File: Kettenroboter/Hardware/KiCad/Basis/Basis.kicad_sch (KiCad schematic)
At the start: 3 parts, among them U2 NCP1117LPST33T3G

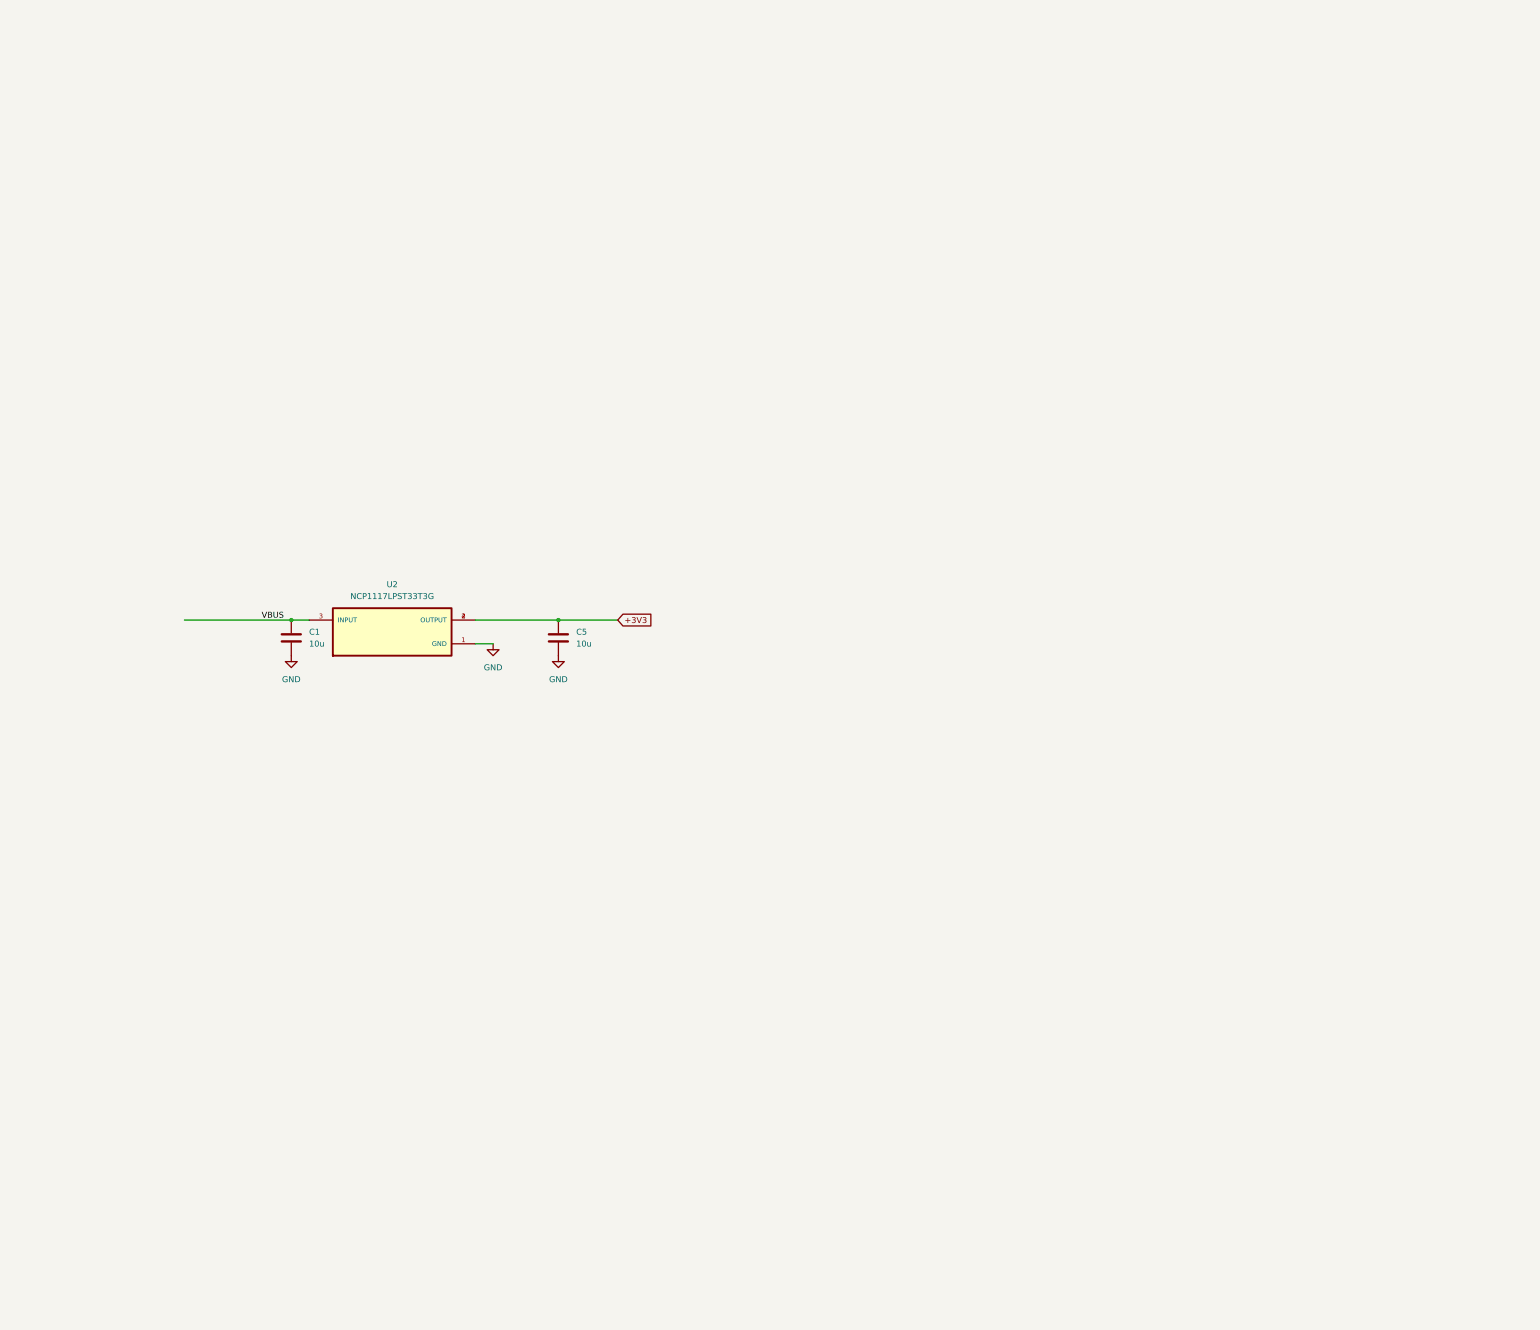
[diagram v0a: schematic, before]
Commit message: Zum Commit vorgemerkte Änderungen: 	neue Datei:     KiCad/Basis/Basis-backups/Basis-2026-01-28_145330.zip 	neue Datei:     KiCad/Basis/Basis-backups/Basis-2026-01-28_151514.zip 	neue Datei:     KiCad/Basis/Basis-backups/Basis-2026-01-28_153414.zip 	neue Datei:     KiCad/Basis/Basis-backups/Basis-2026-01-28_154223.zip 	neue Datei:     KiCad/Basis/Basis-backups/Basis-2026-01-28_155344.zip 	neue Datei:     KiCad/Basis/Basis-backups/Basis-2026-01-29_134332.zip 	neue Datei:     KiCad/Basis/Basis-backups/Basis-2026-01-29_135447.zip 	neue Datei:     KiCad/Basis/Basis-backups/Basis-2026-01-29_141859.zip 	neue Datei:     KiCad/Basis/Basis-backups/Basis-2026-01-29_143547.zip 	neue Datei:     KiCad/Basis/Basis-backups/Basis-2026-01-29_144309.zip 	neue Datei:     KiCad/Basis/Basis-backups/Basis-2026-02-04_130028.zip 	neue Datei:     KiCad/Basis/Basis-backups/Basis-2026-02-04_131400.zip 	neue Datei:     KiCad/Basis/Basis-backups/Basis-2026-02-04_132235.zip 	neue Datei:     KiCad/Basis/Basis-backups/Basis-2026-02-04_132837.zip 	neue Datei:     KiCad/Basis/Basis-backups/Basis-2026-02-04_133547.zip 	neue Datei:     KiCad/Basis/Basis-backups/Basis-2026-02-07_172846.zip 	geändert:       KiCad/Basis/Basis.kicad_pcb 	geändert:       KiCad/Basis/Basis.kicad_prl 	geändert:       KiCad/Basis/Basis.kicad_pro 	geändert:       KiCad/Basis/Basis.kicad_sch 	geändert:       KiCad/Basis/design-block-lib-table 	neue Datei:     KiCad/Basis/fp-info-cache 	neue Datei:     KiCad/Basis/fp-lib-table 	geändert:       KiCad/Basis/sym-lib-table 	geändert:       KiCad/Bausteine/Input_Supply_3V3.kicad_sch 	neue Datei:     KiCad/Bauteil-Library/Buck Converter/buck_conv_place_holder.bak 	neue Datei:     KiCad/Bauteil-Library/Buck Converter/buck_conv_place_holder.kicad_sym 	neue Datei:     KiCad/Bauteil-Library/Footprints/Library.pretty/CONN_39773-0002_MOL.kicad_mod 	neue Datei:     KiCad/Bauteil-Library/Footprints/Library.pretty/Raspberrypi pico2 THT.kicad_mod 	neue Datei:     KiCad/Bauteil-Library/Footprints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
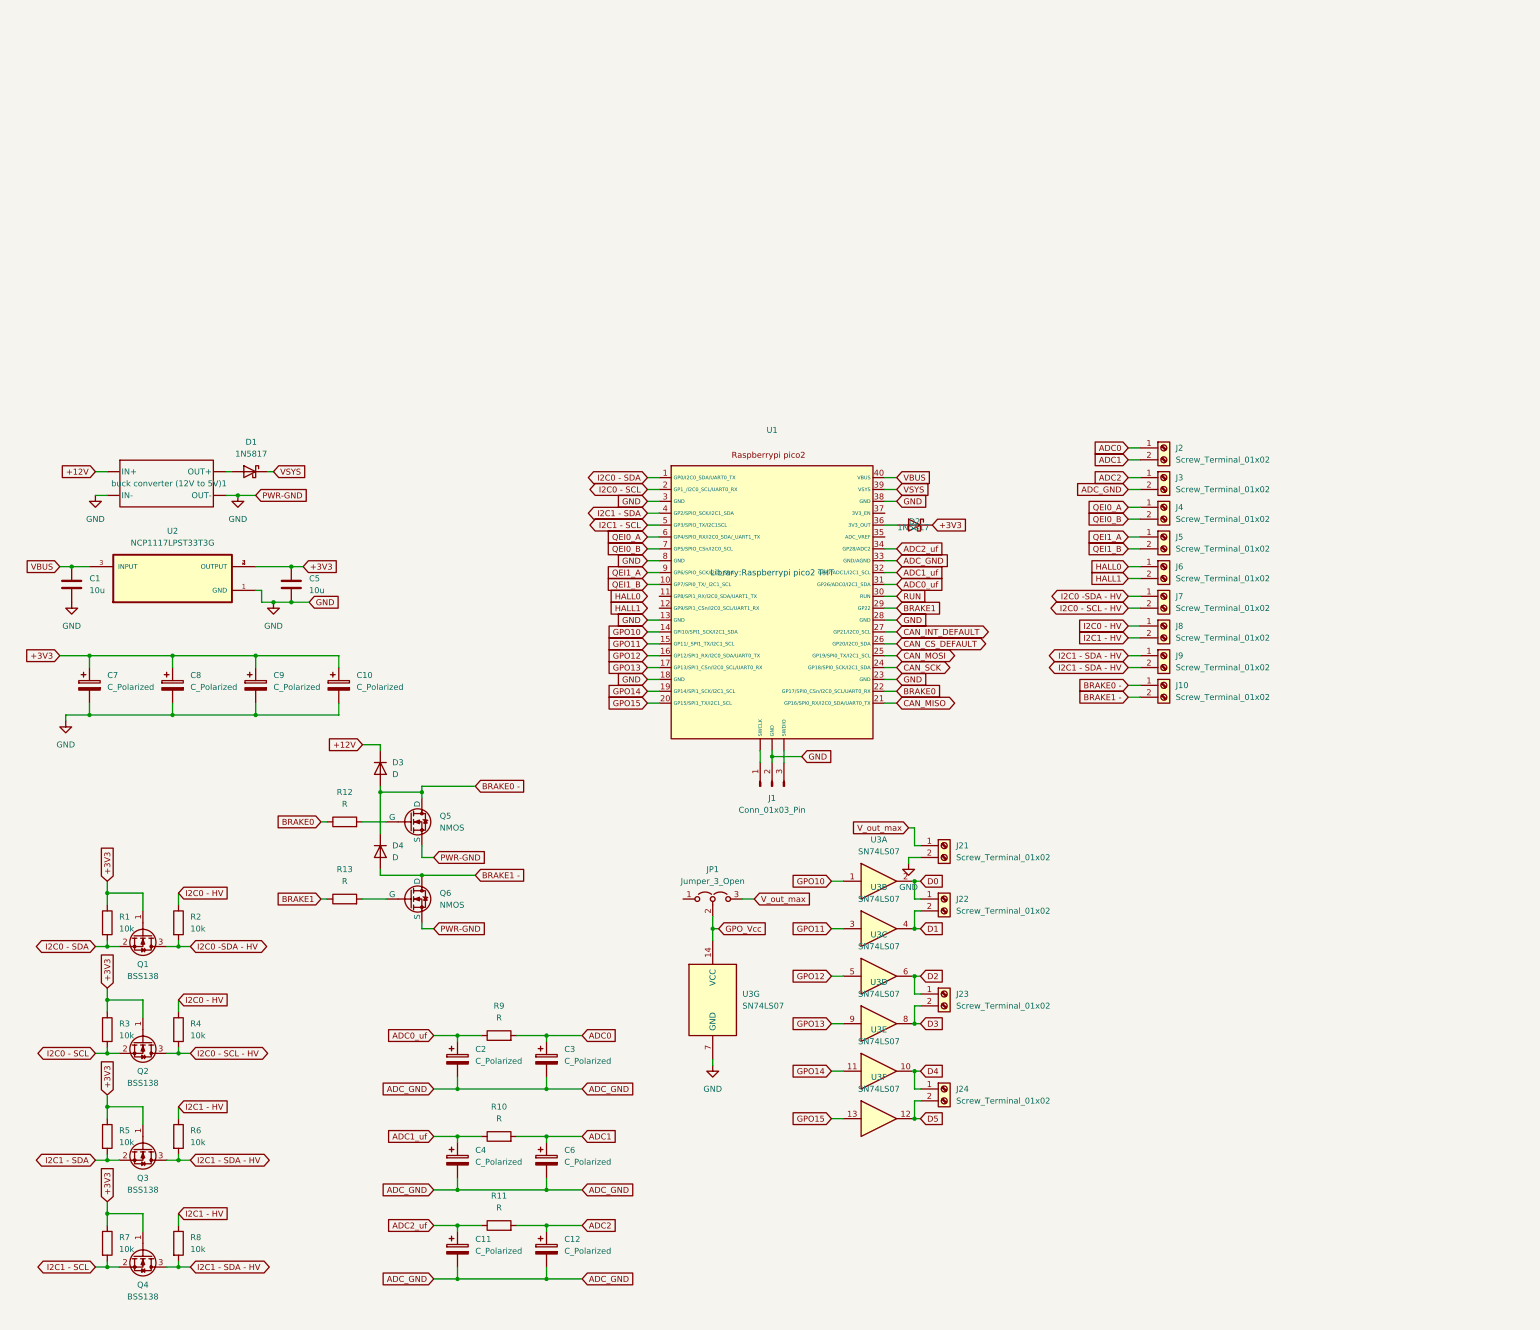
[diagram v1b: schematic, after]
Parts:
- added C10, C11, C12, C2, C3, C4, C6, C7, C8, C9: C_Polarized, symbol Device:C_Polarized
- added D1, D2: 1N5817, Diode_THT:D_DO-41_SOD81_P10.16mm_Horizontal, symbol Diode:1N5817
- added D3, D4: D, symbol Device:D
- added J1: Conn_01x03_Pin, symbol Connector:Conn_01x03_Pin
- added J10, J2, J21, J22, J23, J24, J3, J4, J5, J6, J7, J8, J9: Screw_Terminal_01x02, Library:CONN_39773-0002_MOL, symbol Connector:Screw_Terminal_01x02
- added JP1: Jumper_3_Open, symbol Jumper:Jumper_3_Open
- added Q1, Q2, Q3, Q4: BSS138, Package_TO_SOT_SMD:SOT-23, symbol Transistor_FET:BSS138
- added Q5, Q6: NMOS, Library:SOT-23_AO3400, symbol Simulation_SPICE:NMOS
- added R1, R2, R3, R4, R5, R6, R7, R8: 10k, Resistor_SMD:R_1206_3216Metric_Pad1.30x1.75mm_HandSolder, symbol Device:R
- added R10, R11, R12, R13, R9: R, Resistor_SMD:R_1206_3216Metric_Pad1.30x1.75mm_HandSolder, symbol Device:R
- added U1: ~, Library:Raspberrypi pico2 THT, symbol BA_Pico_2_W:U
- added U3: SN74LS07, Library:SOIC127P600X175-14N, symbol 74xx:SN74LS07
- added buck converter (12V to 5V)1: ~, symbol buck_conv_place_holder:buck_conv_12V_5V_ph
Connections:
- net +3V3: now also C10.1, C7.1, C8.1, C9.1, D2.1 (K), Q1.1 (G), Q2.1 (G), Q3.1 (G), Q4.1 (G), R1.1, R3.1, R5.1, R7.1
- net GND: now also C10.2, C7.2, C8.2, C9.2, J1.2 (Pin_2), J21.2 (Pin_2), Q5.3 (S), Q6.3 (S), U1. (SWDIO), U1.13 (GND), U1.18 (GND), U1.23 (GND), U1.28 (GND), U1.3 (GND), U1.38 (GND), U1.8 (GND), U3.7 (GND), buck converter (12V to 5V)1. (OUT-)
- net VBUS: now also U1.40 (VBUS)
- new net: Q5.2 (G), R12.2
- new net: J1.1 (Pin_1), U1. (SWDIO)
- new net: J1.3 (Pin_3), U1. (SWDIO)
- new net: D1.2 (A), buck converter (12V to 5V)1. (OUT-)
- new net: D2.2 (A), U1.36 (3V3_OUT)
- new net: Q6.2 (G), R13.2
- new net +12V: D3.1 (K), buck converter (12V to 5V)1. (OUT-)
- new net ADC0: C3.1, J2.1 (Pin_1), R9.2
- new net ADC0_uf: C2.1, R9.1, U1.31 (GP26/ADC0/I2C1_SDA)
- new net ADC1: C6.1, J2.2 (Pin_2), R10.2
- new net ADC1_uf: C4.1, R10.1, U1.32 (GP27/ADC1/I2C1_SCL)
- new net ADC2: C12.1, J3.1 (Pin_1), R11.2
- new net ADC2_uf: C11.1, R11.1, U1.34 (GP28/ADC2)
- new net ADC_GND: C11.2, C12.2, C2.2, C3.2, C4.2, C6.2, J3.2 (Pin_2), U1.33 (GND/AGND)
- new net BRAKE0: R12.1, U1.22 (GP17/SPI0_CSn/I2C0_SCL/UART0_RX)
- new net BRAKE0 -: D3.2 (A), D4.1 (K), J10.1 (Pin_1), Q5.1 (D)
- new net BRAKE1: R13.1, U1.29 (GP22)
- new net BRAKE1 -: D4.2 (A), J10.2 (Pin_2), Q6.1 (D)
- new net CAN_CS_DEFAULT: U1.26 (GP20/I2C0_SDA)
- new net CAN_INT_DEFAULT: U1.27 (GP21/I2C0_SCL)
- new net CAN_MISO: U1.21 (GP16/SPI0_RX/I2C0_SDA/UART0_TX)
- new net CAN_MOSI: U1.25 (GP19/SPI0_TX/I2C1_SCL)
- new net CAN_SCK: U1.24 (GP18/SPI0_SCK/I2C1_SDA)
- new net D0: J22.1 (Pin_1), U3.2
- new net D1: J22.2 (Pin_2), U3.4
- new net D2: J23.1 (Pin_1), U3.6
- new net D3: J23.2 (Pin_2), U3.8
- new net D4: J24.1 (Pin_1), U3.10
- new net D5: J24.2 (Pin_2), U3.12
- new net GPO10: U1.14 (GPI10/SPI1_SCK/I2C1_SDA), U3.1
- new net GPO11: U1.15 (GP11/_SPI1_TX/I2C1_SCL), U3.3
- new net GPO12: U1.16 (GP12/SPI1_RX/I2C0_SDA/UART0_TX), U3.5
- new net GPO13: U1.17 (GP13/SPI1_CSn/I2C0_SCL/UART0_RX), U3.9
- new net GPO14: U1.19 (GP14/SPI1_SCK/I2C1_SCL), U3.11
- new net GPO15: U1.20 (GP15/SPI1_TX/I2C1_SCL), U3.13
- new net GPO_Vcc: JP1.2 (C), U3.14 (VCC)
- new net HALL0: J6.1 (Pin_1)
- new net HALL1: J6.2 (Pin_2)
- new net I2C0 - HV: J8.1 (Pin_1), R2.1, R4.1
- new net I2C0 - SCL: Q2.2 (S), R3.2, U1.2 (GP1_/I2C0_SCL/UART0_RX)
- new net I2C0 - SCL - HV: J7.2 (Pin_2), Q2.3 (D), R4.2
- new net I2C0 - SDA: Q1.2 (S), R1.2, U1.1 (GP0/I2C0_SDA/UART0_TX)
- new net I2C0 -SDA - HV: J7.1 (Pin_1), Q1.3 (D), R2.2
- new net I2C1 - HV: J8.2 (Pin_2), R6.1, R8.1
- new net I2C1 - SCL: Q4.2 (S), R7.2, U1.5 (GP3/SPIO_TX/I2C1SCL)
- new net I2C1 - SDA: Q3.2 (S), R5.2, U1.4 (GP2/SPIO_SCK/I2C1_SDA)
- new net I2C1 - SDA - HV: J9.1 (Pin_1), J9.2 (Pin_2), Q3.3 (D), Q4.3 (D), R6.2, R8.2
- new net QEI0_A: J4.1 (Pin_1), U1.6 (GP4/SPIO_RX/I2C0_SDA/_UART1_TX)
- new net QEI0_B: J4.2 (Pin_2), U1.7 (GP5/SPIO_CSn/I2C0_SCL)
- new net QEI1_A: J5.1 (Pin_1), U1.9 (GP6/SPIO_SCK/I2C1_SDA)
- new net QEI1_B: J5.2 (Pin_2), U1.10 (GP7/SPI0_TX/_I2C1_SCL)
- new net RUN: U1.30 (RUN)
- new net VSYS: D1.1 (K), U1.39 (VSYS)
- new net V_out_max: J21.1 (Pin_1), JP1.3 (B)
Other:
- moved on the sheet: C1, C5, U2

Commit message: Nets korrigiert, etc
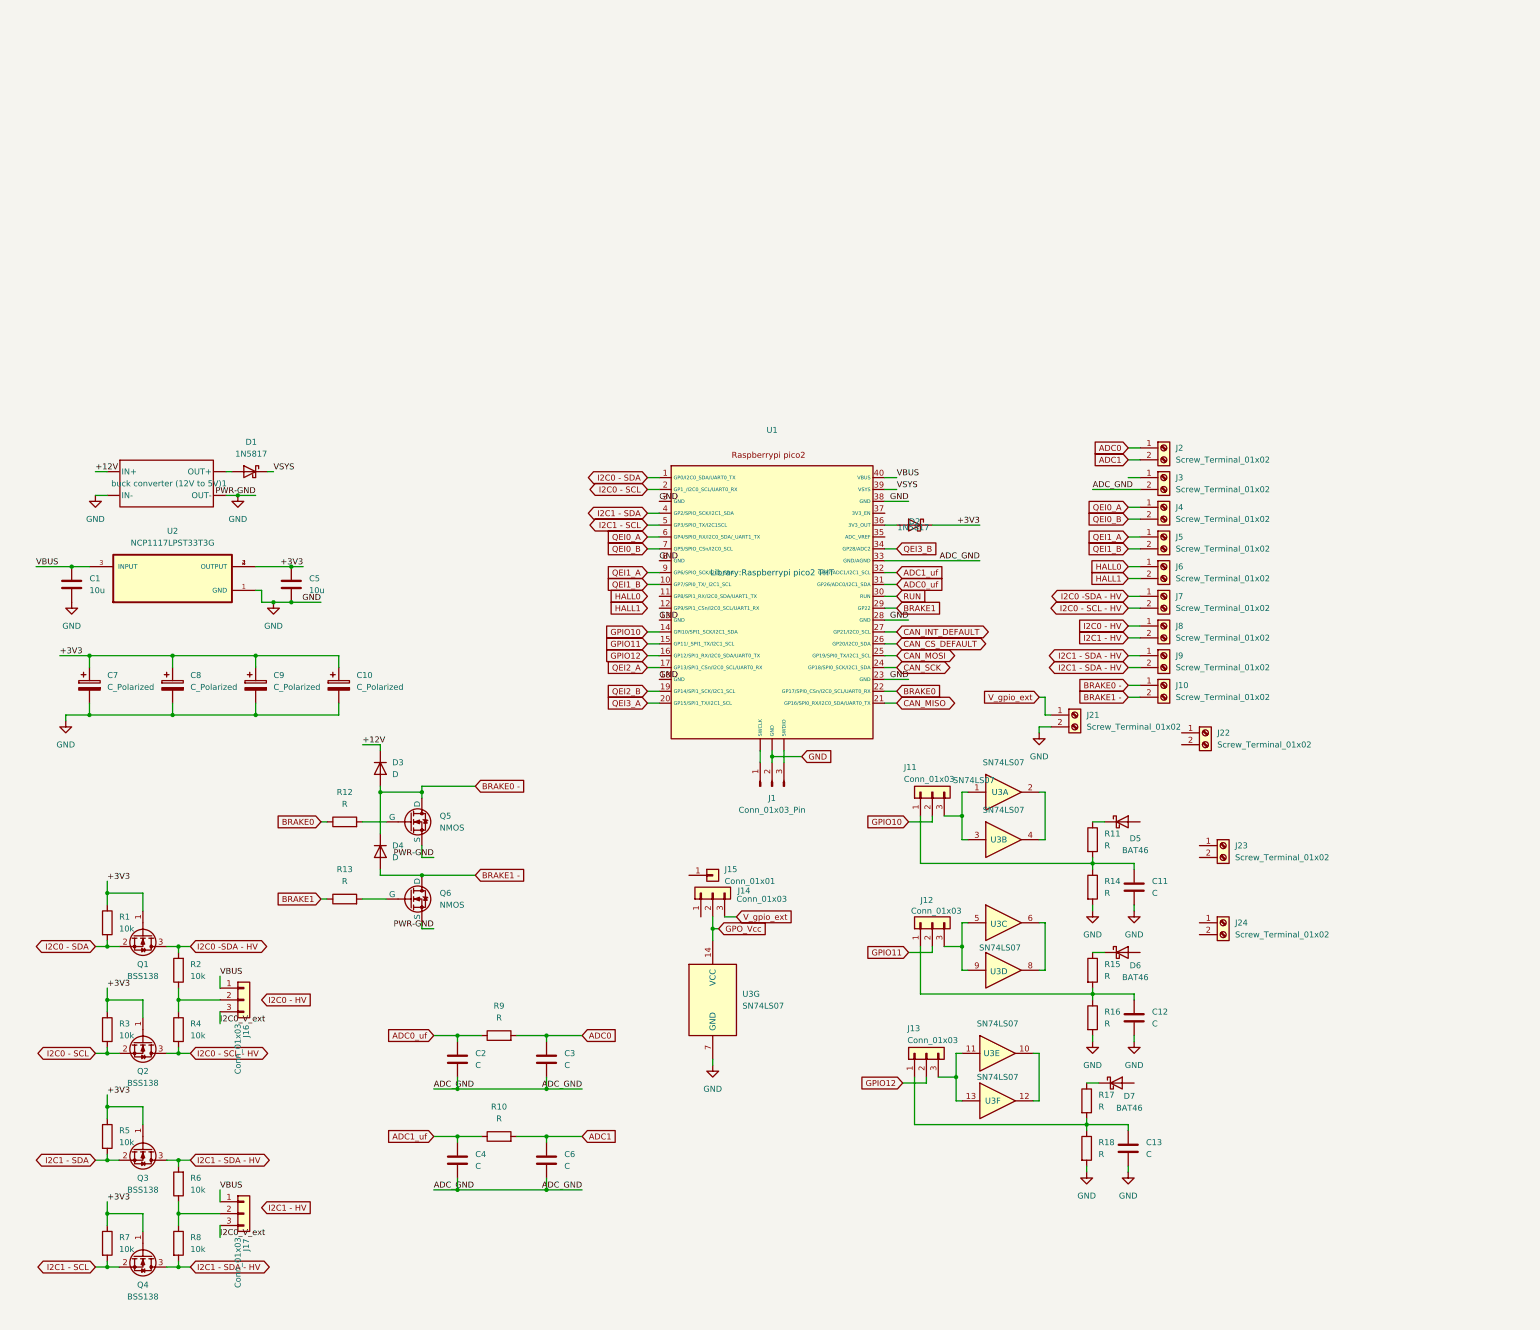
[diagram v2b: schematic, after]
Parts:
- removed C11, C12, C2, C3, C4, C6: C_Polarized, symbol Device:C_Polarized
- removed JP1: Jumper_3_Open, symbol Jumper:Jumper_3_Open
- added C11, C12, C13: C, symbol Device:C
- added C2, C3, C4, C6: C, Capacitor_SMD:C_1206_3216Metric_Pad1.33x1.80mm_HandSolder, symbol Device:C
- added D5, D6, D7: BAT46, Diode_THT:D_DO-35_SOD27_P7.62mm_Horizontal, symbol Diode:BAT46
- added J11, J12, J13, J14, J16, J17: Conn_01x03, symbol Connector_Generic:Conn_01x03
- added J15: Conn_01x01, symbol Connector_Generic:Conn_01x01
- added R14, R15, R16, R17, R18: R, symbol Device:R
- R11: footprint Resistor_SMD:R_1206_3216Metric_Pad1.30x1.75mm_HandSolder -> (none)
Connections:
- net ADC0: now also C3.1
- net ADC0_uf: now also C2.1
- net ADC1: now also C6.1
- net ADC1_uf: now also C4.1
- net ADC_GND: now also C2.2, C3.2, C4.2, C6.2
- net GND: now also C11.2, C12.2, C13.2, R14.2, R16.2, R18.2
- net GPO_Vcc: now also J14.2 (Pin_2)
- net I2C0 - HV: no longer R2.1, R4.1
- net I2C1 - HV: no longer R6.1, R8.1
- net VBUS: now also J16.1 (Pin_1), J17.1 (Pin_1)
- net ADC2: no longer names the net of R11.2
- net ADC2: now also C11.1, J11.1 (Pin_1), R14.1; no longer J3.1 (Pin_1)
- net ADC2_uf: no longer names the net of R11.1
- net ADC2_uf: now also D5.1 (K); no longer U1.34 (GP28/ADC2)
- net D0: no longer names the net of U3.2
- net D0: now also U3.4; no longer J22.1 (Pin_1)
- net D1: no longer names the net of J22.2 (Pin_2)
- net D1: no longer U3.4
- net D2: no longer names the net of U3.6
- net D2: now also U3.8; no longer J23.1 (Pin_1)
- net D3: no longer names the net of J23.2 (Pin_2)
- net D3: no longer U3.8
- net D4: no longer names the net of U3.10
- net D4: now also U3.12; no longer J24.1 (Pin_1)
- net D5: no longer names the net of J24.2 (Pin_2)
- net D5: no longer U3.12
- net GPO10: no longer names the net of U3.1
- net GPO10: now also U3.3, J11.3 (Pin_3); no longer U1.14 (GPI10/SPI1_SCK/I2C1_SDA)
- net GPO11 renamed GPIO11
- net GPIO11: now also J12.2 (Pin_2); no longer U3.3
- net GPO12: no longer names the net of U3.5
- net GPO12: now also U3.9, J12.3 (Pin_3); no longer U1.16 (GP12/SPI1_RX/I2C0_SDA/UART0_TX)
- net GPO13 renamed QEI2_A
- net QEI2_A: no longer U3.9
- net GPO14: no longer names the net of U3.11
- net GPO14: now also U3.13, J13.3 (Pin_3); no longer U1.19 (GP14/SPI1_SCK/I2C1_SCL)
- net GPO15 renamed QEI3_A
- net QEI3_A: no longer U3.13
- net V_out_max renamed V_gpio_ext
- net V_gpio_ext: now also J14.3 (Pin_3)
- new net: C13.1, J13.1 (Pin_1), R17.2, R18.1
- new net: J17.2 (Pin_2), R6.1, R8.1
- new net: D6.1 (K), R15.1
- new net: C12.1, J12.1 (Pin_1), R15.2, R16.1
- new net: J16.2 (Pin_2), R2.1, R4.1
- new net: D7.1 (K), R17.1
- new net GPIO10: J11.2 (Pin_2), U1.14 (GPI10/SPI1_SCK/I2C1_SDA)
- new net GPIO12: J13.2 (Pin_2), U1.16 (GP12/SPI1_RX/I2C0_SDA/UART0_TX)
- new net I2C0_V_ext: J16.3 (Pin_3), J17.3 (Pin_3)
- new net QEI2_B: U1.19 (GP14/SPI1_SCK/I2C1_SCL)
- new net QEI3_B: U1.34 (GP28/ADC2)
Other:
- moved on the sheet: J21, J22, J23, J24, R2, R6, U3A, U3B, U3C, U3D, U3E, U3F
